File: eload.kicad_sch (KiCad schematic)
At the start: 52 parts, among them J1 Device Power, J2 Input, J3 JST Header, J4 SWD Header, J7 Conn_02x06_Odd_Even, K1 G5Q-1, Q1 TIP122, Q2 HL 40N05, Q4 DTC043Z, SW1 SW_Push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

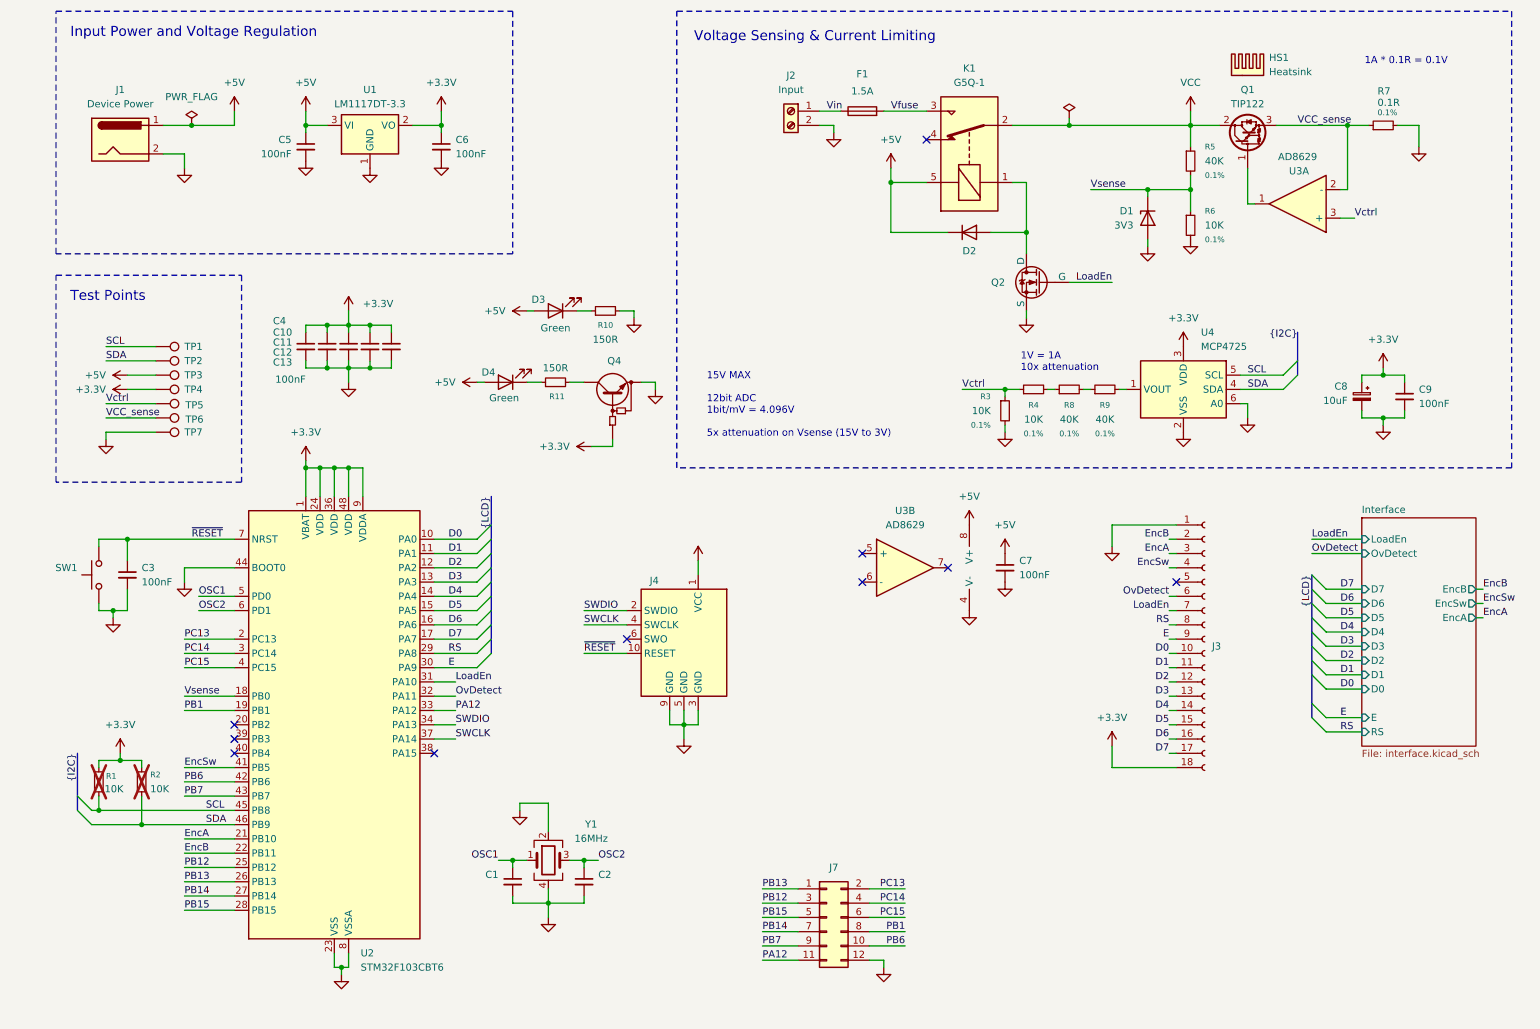
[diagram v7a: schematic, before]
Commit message: 3D models added, mounting holes added
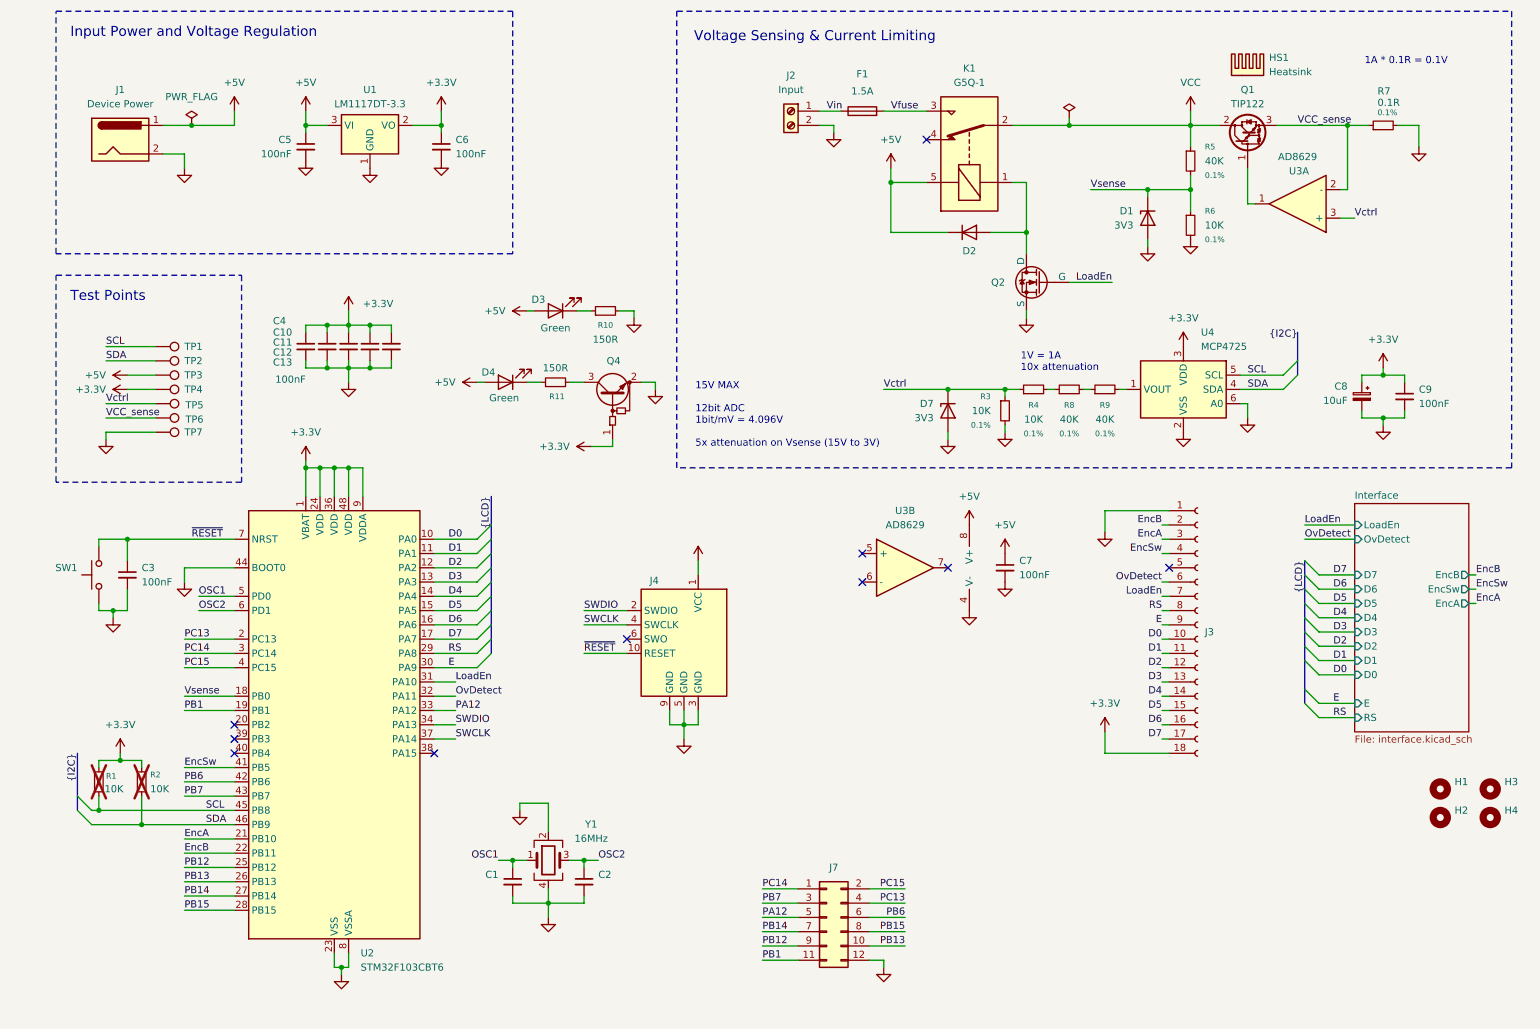
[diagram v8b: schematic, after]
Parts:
- added D7: BZT52C3V3S, Diode_SMD:D_SOD-323_HandSoldering, symbol Device:D_Zener
- added H1, H2, H3, H4: MountingHole, MountingHole:MountingHole_3.2mm_M3_DIN965, symbol Mechanical:MountingHole
- D2: footprint (none) -> Diode_SMD:D_SOD-123F
- HS1: footprint (none) -> eload:XSD1226-362
- J2: footprint Connector:Banana_Jack_2Pin -> TerminalBlock_CUI:TerminalBlock_CUI_TB007-508-02_1x02_P5.08mm_Horizontal
- Q4: footprint (none) -> Package_TO_SOT_SMD:SOT-416; symbol Device:Q_NPN_BRT -> Transistor_BJT:Q_NPN_BRT_BEC
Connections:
- net +3.3V: now also Q4.1 (B); no longer Q4.B
- net GND: now also Q4.2 (E), D7.2 (A); no longer Q4.E
- net PA12: now also J7.5 (Pin_5); no longer J7.11 (Pin_11)
- net PB1: now also J7.11 (Pin_11); no longer J7.8 (Pin_8)
- net PB12: now also J7.9 (Pin_9); no longer J7.3 (Pin_3)
- net PB13: now also J7.10 (Pin_10); no longer J7.1 (Pin_1)
- net PB15: now also J7.8 (Pin_8); no longer J7.5 (Pin_5)
- net PB6: now also J7.6 (Pin_6); no longer J7.10 (Pin_10)
- net PB7: now also J7.3 (Pin_3); no longer J7.9 (Pin_9)
- net PC13: now also J7.4 (Pin_4); no longer J7.2 (Pin_2)
- net PC14: now also J7.1 (Pin_1); no longer J7.4 (Pin_4)
- net PC15: now also J7.2 (Pin_2); no longer J7.6 (Pin_6)
- net Vctrl: now also D7.1 (K)
- net at R11.2: now also Q4.3 (C); no longer Q4.C
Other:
- moved on the sheet: J3
